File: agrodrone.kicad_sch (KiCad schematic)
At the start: 52 parts, among them J1 HDR-2.54, J10 HDR-2.54, J11 Conn_01x03, J12 Conn_01x01, J13 HDR-2.54, J14 Conn_01x01, J15 HDR-2.54, J2 Conn_01x01, J3 HDR-2.54, J4 HDR-2.54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

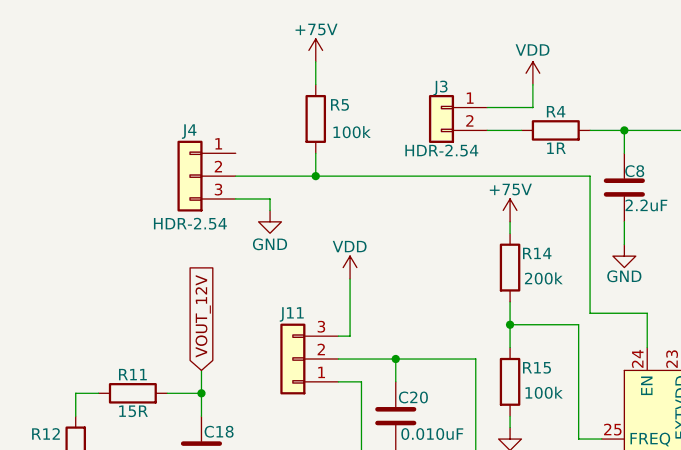
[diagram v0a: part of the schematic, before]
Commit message: Добавил STM32 и измерения
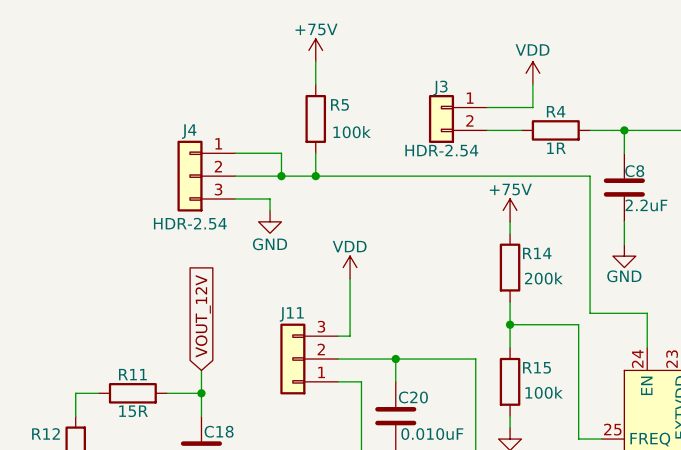
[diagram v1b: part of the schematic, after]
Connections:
- net at J4.1 (Pin_1): now also J4.2 (Pin_2), R5.2, U1.24 (EN)
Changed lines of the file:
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@@
+	)
+	(junction
+		(at 50.8 46.99)
+		(diameter 0)
+		(color 0 0 0 0)
 	)
 	(junction
@@
 	(wire
 		(pts
+			(xy 50.8 44.45) (xy 50.8 46.99)
+		)
+		(stroke
+			(width 0)
+			(type default)
+		)
+	)
+	(wire
+		(pts
 			(xy 72.39 80.01) (xy 72.39 67.31)
 		)
@@
 	(wire
 		(pts
+			(xy 50.8 46.99) (xy 54.61 46.99)
+		)
+		(stroke
+			(width 0)
+			(type default)
+		)
+	)
+	(wire
+		(pts
 			(xy 83.82 76.2) (xy 83.82 63.5)
 		)
@@
 	(wire
 		(pts
-			(xy 45.72 46.99) (xy 54.61 46.99)
+			(xy 45.72 46.99) (xy 50.8 46.99)
 		)
 		(stroke
@@
 		)
 		(stroke
+			(width 0)
+			(type default)
+		)
+	)
+	(wire
+		(pts
+			(xy 45.72 44.45) (xy 50.8 44.45)
+		)
+		(stroke
